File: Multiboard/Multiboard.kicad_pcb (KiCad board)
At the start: 2 copper layers, 150 x 120 mm, 192 parts, among them J1 Conn_01x20_Socket, J2 Conn_01x20_Socket, J3 Debug, J4 USB_C_Receptacle_USB2.0_16P, J5 Conn_01x06_Socket, J6 Conn_02x20_Odd_Even, J7 Conn_02x20_Odd_Even, J8 USB_C_Receptacle_USB2.0_16P, Q1 Q_Dual_NMOS_G1S2G2D2S1D1, Q2 Q_Dual_NMOS_G1S2G2D2S1D1, Q3 Q_Dual_NMOS_G1S2G2D2S1D1, Q4 Q_Dual_NMOS_G1S2G2D2S1D1, Q5 Q_Dual_NMOS_G1S2G2D2S1D1, Q6 Q_Dual_NMOS_G1S2G2D2S1D1, Q7 Q_Dual_NMOS_G1S2G2D2S1D1, SW1 BOOT0, SW2 NRST, SW3 SW_SPST, SW4 SW_SPST, SW5 SW_SPST, SW6 SW_SPST, SW7 KEY, SW8 SW_SPST, U1 STM32F411RET6, U2 MAX662AESA_T, U3 MCP1792x-3302xCB, U4 FT2232HL-REEL, U5 93LCxxC, U6 LCMXO2-1200ZE-1TG144C, U7 FAN1112, U8 NCP1117, Y1 32.768KHz, Y2 25MHz, Y3 12MHz

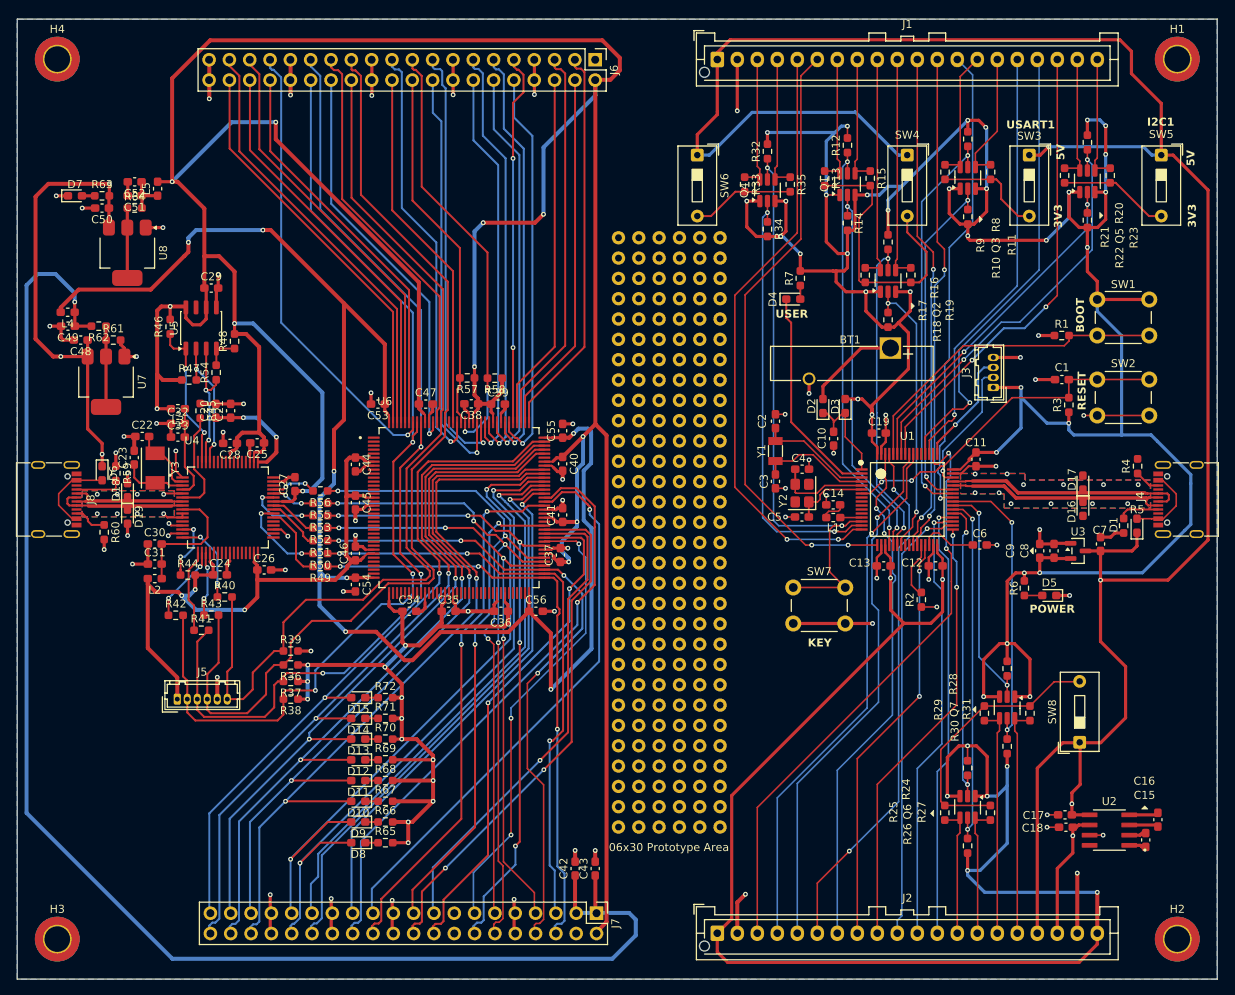
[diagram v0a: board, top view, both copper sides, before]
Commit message: added elsys logo and project name to silkscreen
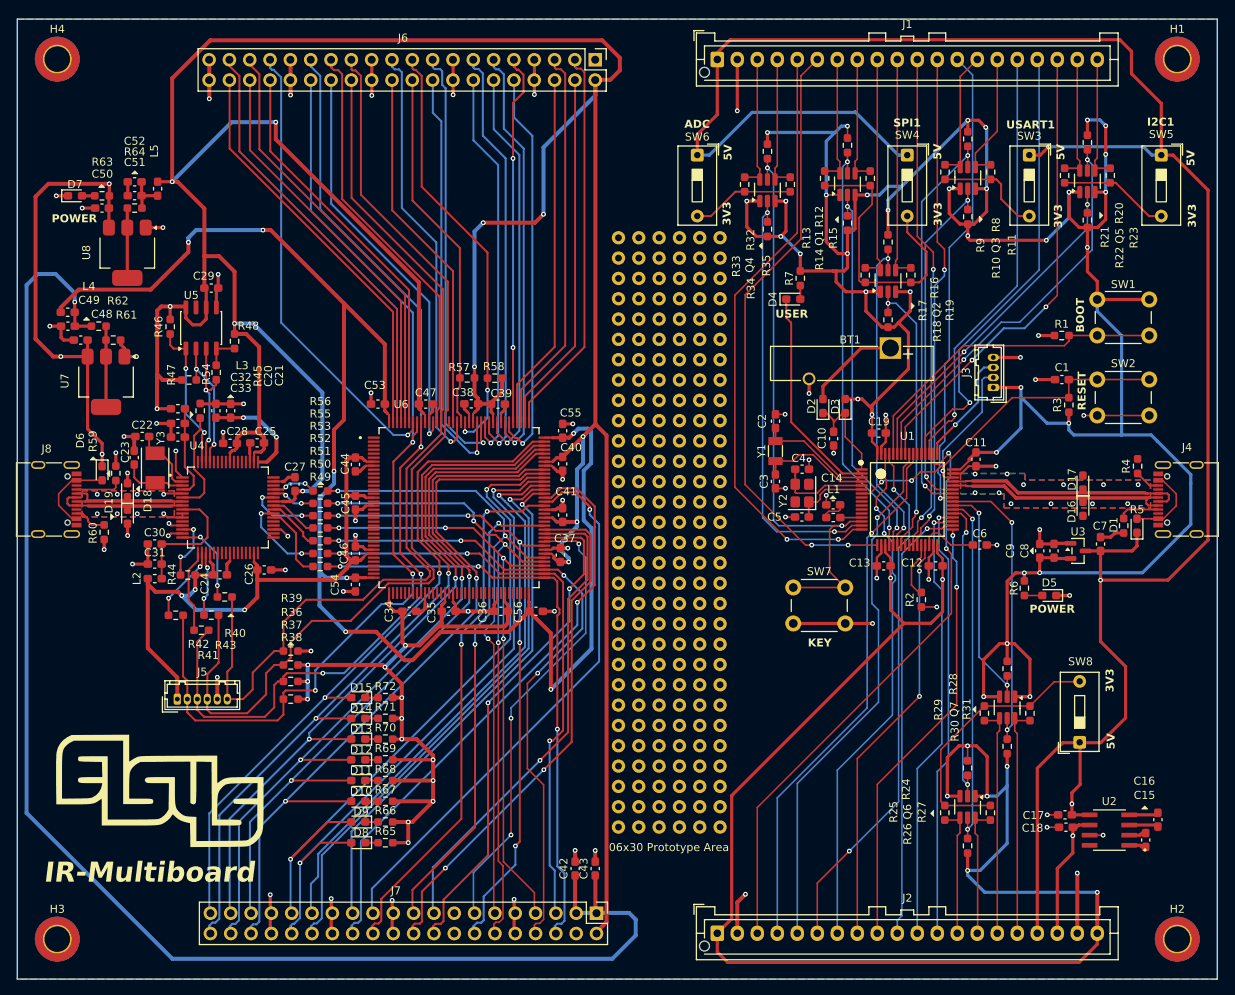
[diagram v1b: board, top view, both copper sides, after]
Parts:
- added G***: LOGO, LOGO, F.Cu at (82.3, 134.2)
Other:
- board text added: "ADC"
- board text added: "IR-Multiboard"
- board text added: "SPI1"

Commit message: fixed trace spacing issues in fpga pins
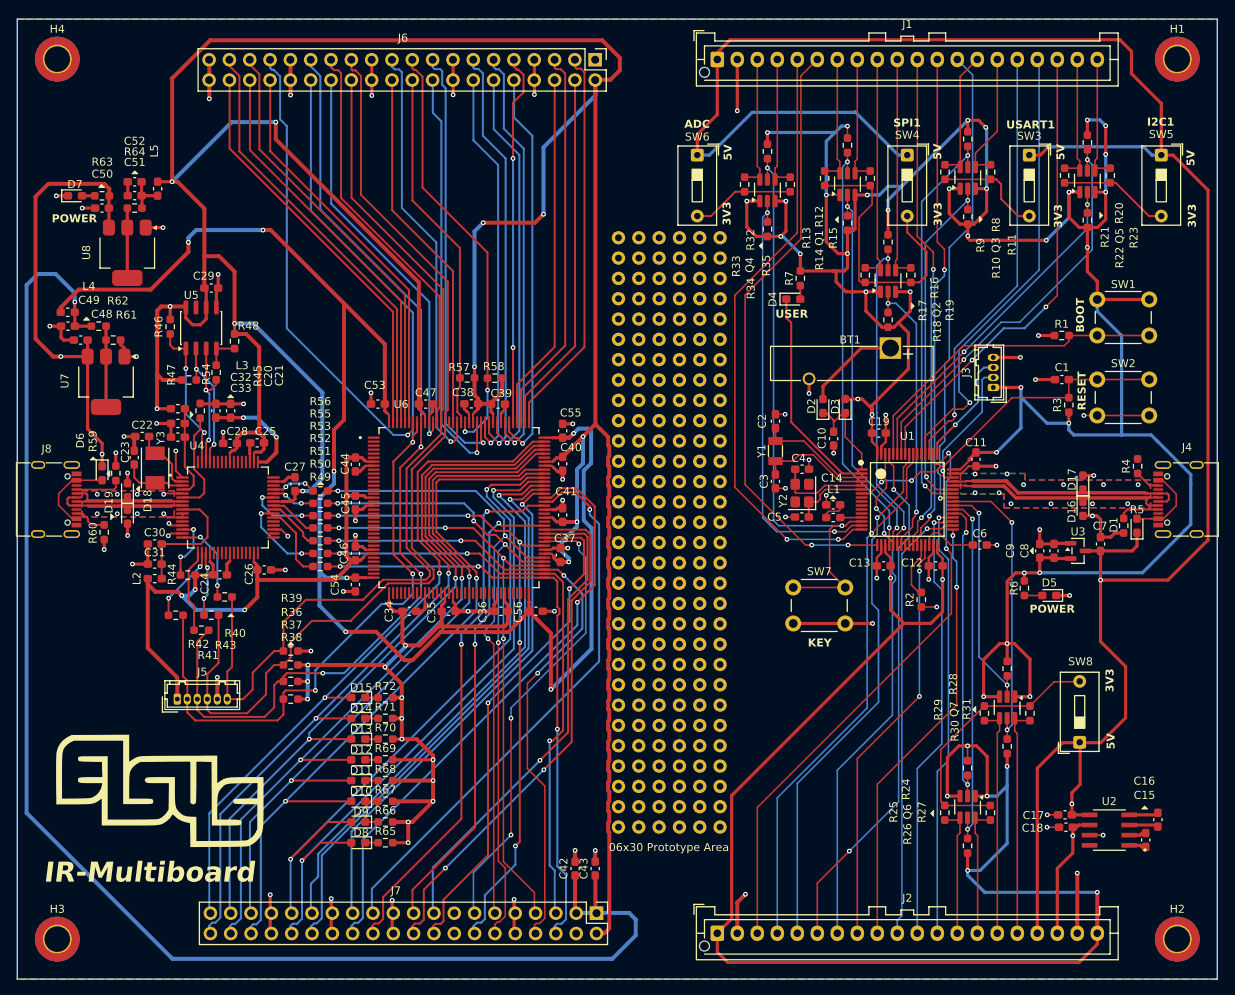
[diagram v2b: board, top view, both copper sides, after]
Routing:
- net GND: track 254.2 -> 260.0 mm, vias 89 -> 91
- net 3V3: track 1200.0 -> 1203.1 mm
- net 5V: track 329.9 -> 329.6 mm, vias 6 -> 5

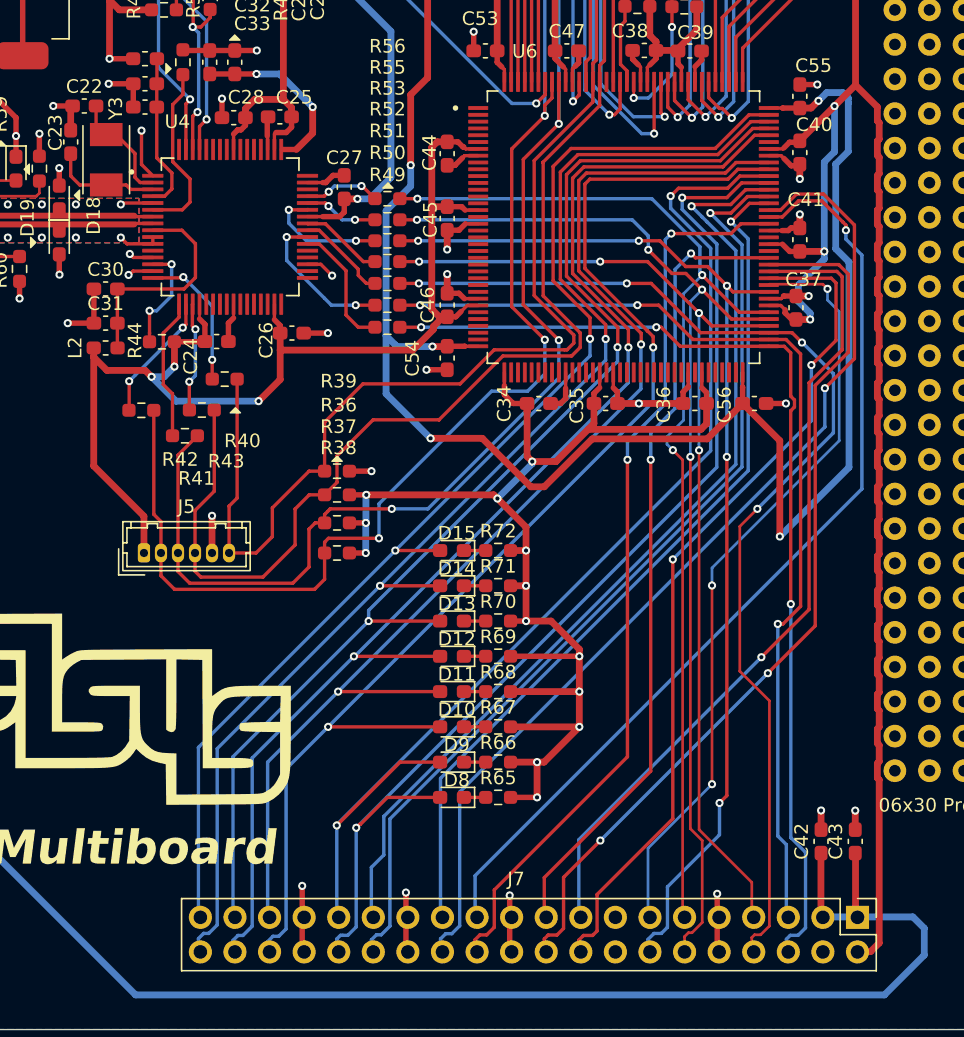
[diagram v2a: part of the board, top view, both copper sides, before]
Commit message: cleared part of errors and warnings
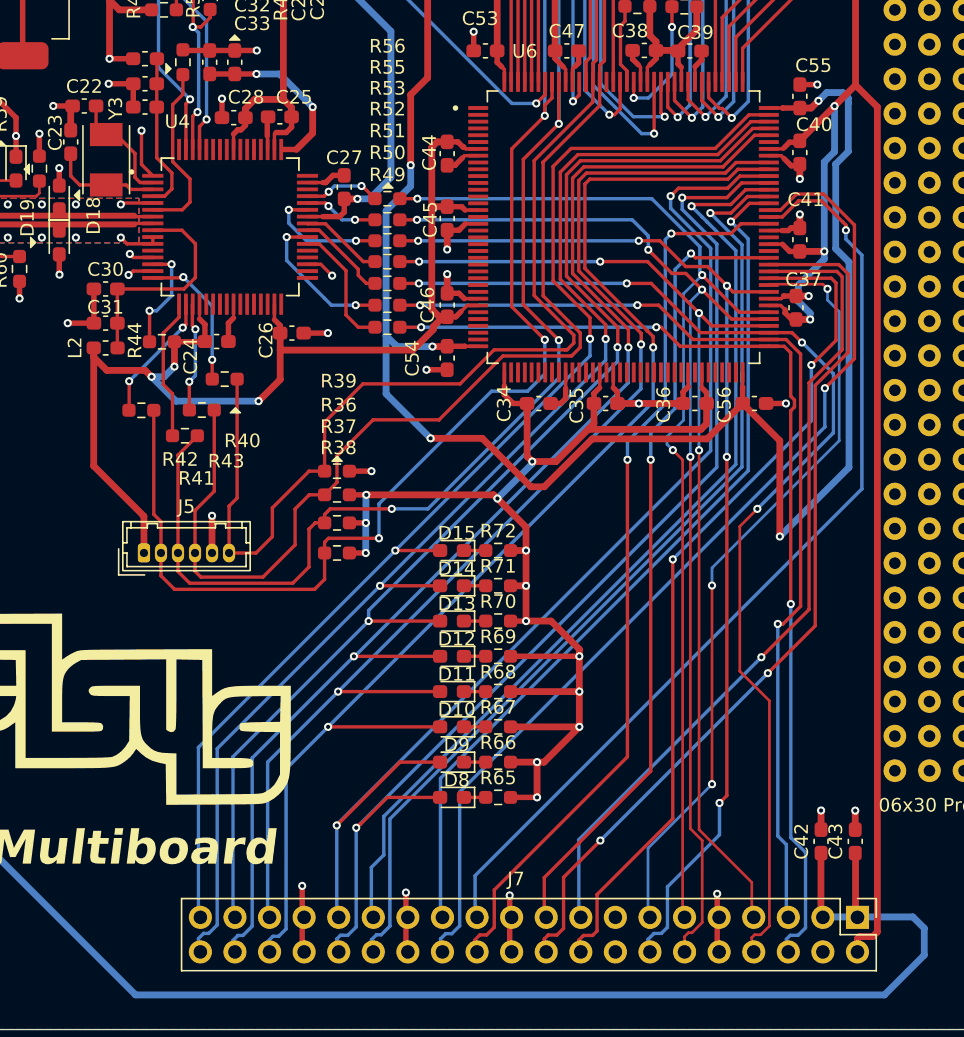
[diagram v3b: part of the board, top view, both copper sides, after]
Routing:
- net 3V3: track 1203.1 -> 1200.8 mm

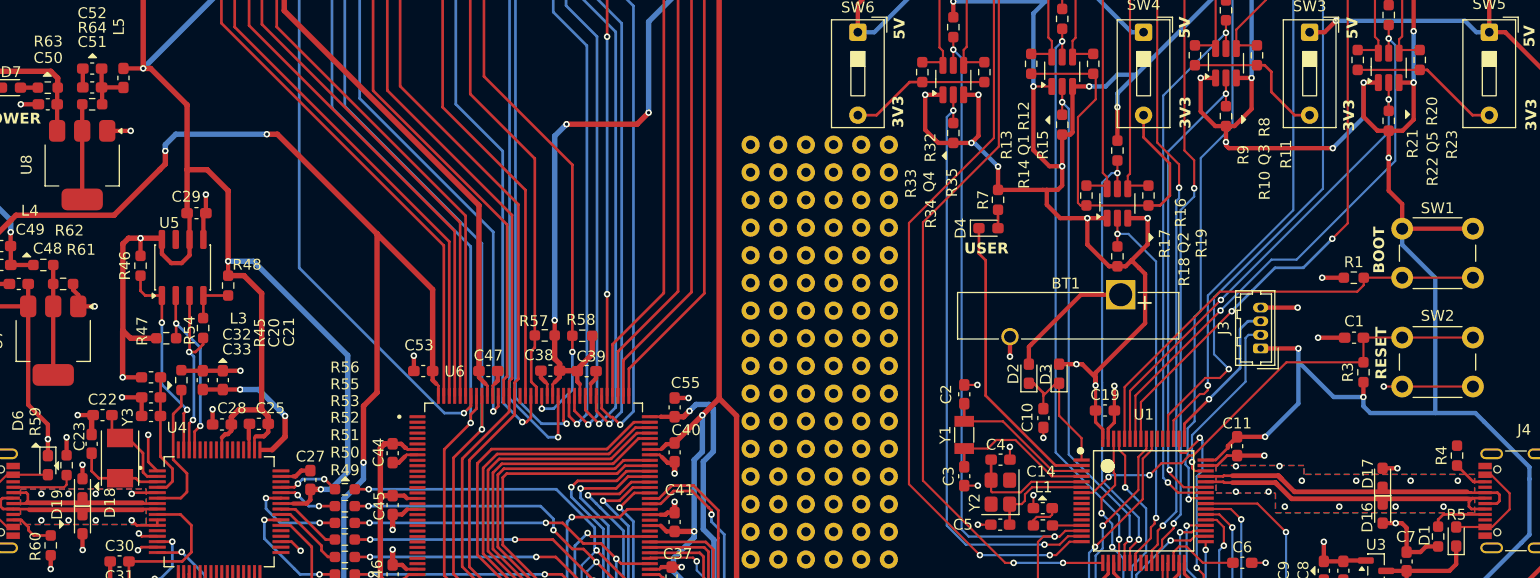
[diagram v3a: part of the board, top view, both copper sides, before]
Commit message: cleared thermal relief and solder mask  errors
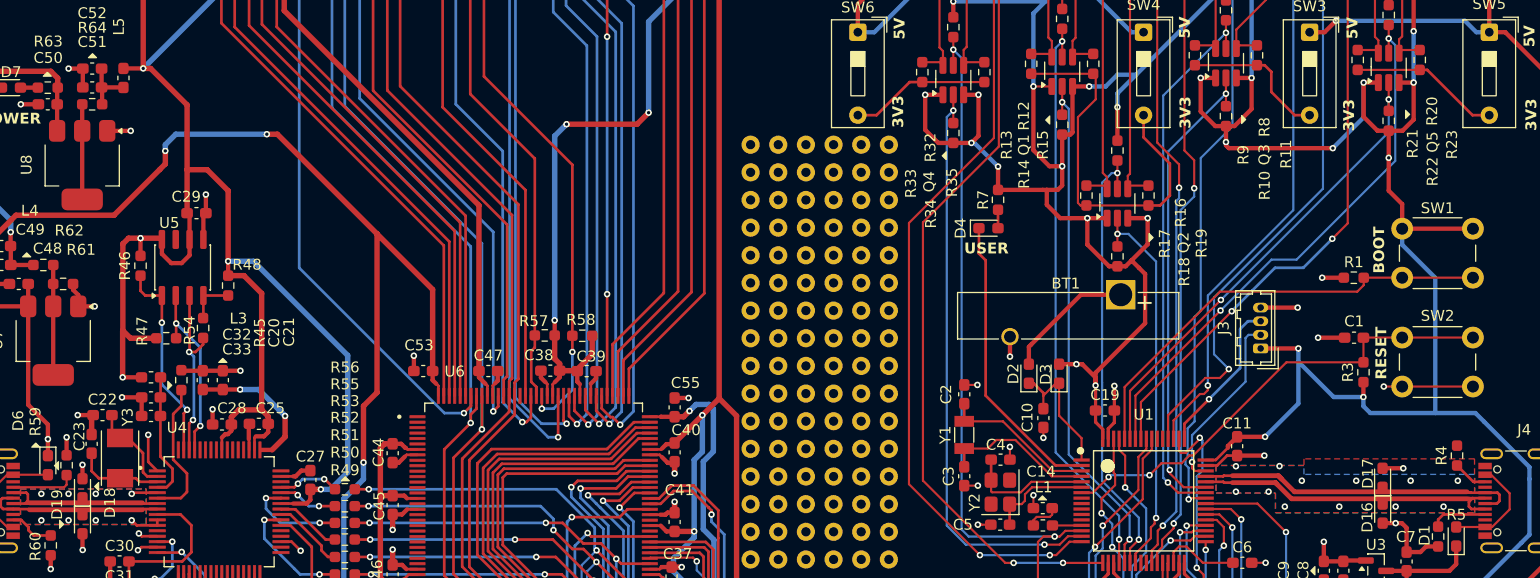
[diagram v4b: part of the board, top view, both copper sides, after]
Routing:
- net GND: track 260.0 -> 261.8 mm, vias 91 -> 92
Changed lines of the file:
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@@
 		(sheetname "/MCU/")
 		(sheetfile "MCU.kicad_sch")
-		(attr smd)
+		(solder_mask_margin 0)
+		(attr smd allow_soldermask_bridges)
 		(fp_line
 			(start -4.6 -4.6)
@@
 	)
 	(segment
+		(start 199.619 94.843)
+		(end 199.622 94.846)
+		(width 0.4)
+		(layer "F.Cu")
+		(net 1)
+	)
+	(segment
 		(start 83.735 101.088)
 		(end 83.479 100.832)
@@
 	)
 	(segment
+		(start 78.329 58.132)
+		(end 77.022 58.132)
+		(width 0.4)
+		(layer "F.Cu")
+		(net 1)
+	)
+	(segment
 		(start 130.409 104.112)
 		(end 131.319 104.112)
@@
 	)
 	(segment
+		(start 197.719 94.843)
+		(end 199.619 94.843)
+		(width 0.4)
+		(layer "F.Cu")
+		(net 1)
+	)
+	(segment
 		(start 91.1 104.518)
 		(end 91.1 105.531)
@@
 	)
 	(segment
-		(start 197.719 94.843)
-		(end 199.081 94.843)
-		(width 0.4)
-		(layer "F.Cu")
-		(net 1)
-	)
-	(segment
 		(start 119.00002 42.838)
 		(end 119.00002 45.378)
@@
 	)
 	(via
+		(at 77.022 58.132)
+		(size 0.6)
+		(drill 0.3)
+		(layers "F.Cu" "B.Cu")
+		(net 1)
+	)
+	(via
 		(at 82.819 97.192)
 		(size 0.6)
@@
 	)
 	(via
-		(at 199.081 94.843)
+		(at 199.622 94.846)
 		(size 0.6)
 		(drill 0.3)
@@
 		(polygon
 			(pts
-				(xy 206.179 98.928) (xy 206.169 95.408) (xy 190.499 95.408) (xy 190.499 94.588) (xy 182.419 94.588)
+				(xy 206.179 98.928) (xy 206.164935 93.98) (xy 190.499 93.98) (xy 190.499 94.588) (xy 182.419 94.588)
 				(xy 182.429 97.128) (xy 187.879 97.128) (xy 187.879 98.928)
 			)
